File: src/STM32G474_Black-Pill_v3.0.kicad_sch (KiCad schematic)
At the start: 47 parts, among them J101 USB_C_Receptacle_USB2.0, J102 Conn_01x20, J103 Conn_01x20, J104 Conn_01x04, SW101 SW_Push, SW102 SW_Push, SW103 SW_Push, U101 W25Q32JVSS, U102 STM32G474CEUx, U103 AP7343xx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

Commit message: Add: Production data
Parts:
- C101, C104, C112, C114, C115, C119, C120: Manufacturer Part no. (none) -> -; Vendor (none) -> From stock; Vendor Part No. (none) -> -
- JP101, JP102, JP103: Manufacturer Part no. (none) -> -; Vendor (none) -> -; Vendor Part No. (none) -> -
- U102: Manufacturer Part no. (none) -> STM32G474CEU6; Vendor (none) -> Digikey; Vendor Part No. (none) -> 497-STM32G474CEU6-ND
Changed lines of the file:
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@@
+      (effects (font (size 1.27 1.27)) hide)
+    )
+    (property "Manufacturer Part no." "-" (at 133.35 184.15 0)
+      (effects (font (size 1.27 1.27)) hide)
+    )
+    (property "Vendor" "From stock" (at 133.35 184.15 0)
+      (effects (font (size 1.27 1.27)) hide)
+    )
+    (property "Vendor Part No." "-" (at 133.35 184.15 0)
       (effects (font (size 1.27 1.27)) hide)
     )
@@
     )
     (property "Datasheet" "~" (at 31.75 184.15 0)
+      (effects (font (size 1.27 1.27)) hide)
+    )
+    (property "Manufacturer Part no." "-" (at 31.75 184.15 0)
+      (effects (font (size 1.27 1.27)) hide)
+    )
+    (property "Vendor" "From stock" (at 31.75 184.15 0)
+      (effects (font (size 1.27 1.27)) hide)
+    )
+    (property "Vendor Part No." "-" (at 31.75 184.15 0)
       (effects (font (size 1.27 1.27)) hide)
     )
@@
       (effects (font (size 1.27 1.27)) hide)
     )
+    (property "Manufacturer Part no." "-" (at 63.5 184.15 0)
+      (effects (font (size 1.27 1.27)) hide)
+    )
+    (property "Vendor" "From stock" (at 63.5 184.15 0)
+      (effects (font (size 1.27 1.27)) hide)
+    )
+    (property "Vendor Part No." "-" (at 63.5 184.15 0)
+      (effects (font (size 1.27 1.27)) hide)
+    )
     (pin "1")
     (pin "2")
@@
       (effects (font (size 1.27 1.27)) hide)
     )
+    (property "Manufacturer Part no." "-" (at 102.87 90.17 0)
+      (effects (font (size 1.27 1.27)) hide)
+    )
+    (property "Vendor" "-" (at 102.87 90.17 0)
+      (effects (font (size 1.27 1.27)) hide)
+    )
+    (property "Vendor Part No." "-" (at 102.87 90.17 0)
+      (effects (font (size 1.27 1.27)) hide)
+    )
     (pin "1")
     (pin "2")
@@
     )
     (property "Datasheet" "https://www.st.com/resource/en/datasheet/stm32g474ce.pdf" (at 165.1 86.36 0)
+      (effects (font (size 1.27 1.27)) hide)
+    )
+    (property "Manufacturer Part no." "STM32G474CEU6" (at 165.1 86.36 0)
+      (effects (font (size 1.27 1.27)) hide)
+    )
+    (property "Vendor" "Digikey" (at 165.1 86.36 0)
+      (effects (font (size 1.27 1.27)) hide)
+    )
+    (property "Vendor Part No." "497-STM32G474CEU6-ND" (at 165.1 86.36 0)
       (effects (font (size 1.27 1.27)) hide)
     )
@@
       (effects (font (size 1.27 1.27)) hide)
     )
+    (property "Manufacturer Part no." "-" (at 110.49 24.13 0)
+      (effects (font (size 1.27 1.27)) hide)
+    )
+    (property "Vendor" "From stock" (at 110.49 24.13 0)
+      (effects (font (size 1.27 1.27)) hide)
+    )
+    (property "Vendor Part No." "-" (at 110.49 24.13 0)
+      (effects (font (size 1.27 1.27)) hide)
+    )
     (pin "1")
     (pin "2")
@@
       (effects (font (size 1.27 1.27)) hide)
     )
+    (property "Manufacturer Part no." "-" (at 146.05 184.15 0)
+      (effects (font (size 1.27 1.27)) hide)
+    )
+    (property "Vendor" "From stock" (at 146.05 184.15 0)
+      (effects (font (size 1.27 1.27)) hide)
+    )
+    (property "Vendor Part No." "-" (at 146.05 184.15 0)
+      (effects (font (size 1.27 1.27)) hide)
+    )
     (pin "1")
     (pin "2")
@@
     )
     (property "Datasheet" "~" (at 102.87 109.22 0)
+      (effects (font (size 1.27 1.27)) hide)
+    )
+    (property "Manufacturer Part no." "-" (at 102.87 109.22 0)
+      (effects (font (size 1.27 1.27)) hide)
+    )
+    (property "Vendor" "-" (at 102.87 109.22 0)
+      (effects (font (size 1.27 1.27)) hide)
+    )
+    (property "Vendor Part No." "-" (at 102.87 109.22 0)
       (effects (font (size 1.27 1.27)) hide)
     )
@@
       (effects (font (size 1.27 1.27)) hide)
     )
+    (property "Manufacturer Part no." "-" (at 264.16 45.72 0)
+      (effects (font (size 1.27 1.27)) hide)
+    )
+    (property "Vendor" "From stock" (at 264.16 45.72 0)
+      (effects (font (size 1.27 1.27)) hide)
+    )
+    (property "Vendor Part No." "-" (at 264.16 45.72 0)
+      (effects (font (size 1.27 1.27)) hide)
+    )
     (pin "1")
     (pin "2")
@@
       (effects (font (size 1.27 1.27)) hide)
     )
+    (property "Manufacturer Part no." "-" (at 107.95 152.4 0)
+      (effects (font (size 1.27 1.27)) hide)
+    )
+    (property "Vendor" "From stock" (at 107.95 152.4 0)
+      (effects (font (size 1.27 1.27)) hide)
+    )
+    (property "Vendor Part No." "-" (at 107.95 152.4 0)
+      (effects (font (size 1.27 1.27)) hide)
+    )
     (pin "1")
     (pin "2")
@@
       (effects (font (size 1.27 1.27)) hide)
     )
+    (property "Manufacturer Part no." "-" (at 67.31 146.05 0)
+      (effects (font (size 1.27 1.27)) hide)
+    )
+    (property "Vendor" "-" (at 67.31 146.05 0)
+      (effects (font (size 1.27 1.27)) hide)
+    )
+    (property "Vendor Part No." "-" (at 67.31 146.05 0)
+      (effects (font (size 1.27 1.27)) hide)
+    )

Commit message: Mod: STM32G474_Black-Pill_v3.0.kicad_sch, updated BOM and re-exported BOM_A.xlsx.
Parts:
- C101, C104, C108, C109, C110, C112, C114, C115, C119, C120: Manufacturer Part no. - -> GRM155R71C104KA88D; Vendor From stock -> Digikey; Vendor Part No. - -> 490-3261-1-ND
- C107: Manufacturer Part no. - -> GRM155R60J106ME15D; Vendor From stock -> Digikey; Vendor Part No. - -> 490-13238-1-ND
- C113, C116, C117, C118: Manufacturer Part no. - -> GRM155C81C105KE11D; Vendor From stock -> Digikey; Vendor Part No. - -> 490-12700-1-ND
- R101, R102: Manufacturer Part no. - -> RC0402FR-075K1L; Vendor From stock -> Digikey; Vendor Part No. - -> 311-5.10KLRCT-ND
- R103, R108: Manufacturer Part no. - -> RC0402FR-0710KL; Vendor From stock -> Digikey; Vendor Part No. - -> 311-10.0KLRCT-ND
- R104, R105: Manufacturer Part no. - -> RC0402FR-0710RL; Vendor From stock -> Digikey; Vendor Part No. - -> 311-10.0LRCT-ND
- R107, R109: Manufacturer Part no. - -> RC0402FR-07100RL; Vendor From stock -> Digikey; Vendor Part No. - -> 311-100LRCT-ND
- R218: Manufacturer Part no. - -> RC0402FR-070RL; Vendor From stock -> Digikey; Vendor Part No. - -> 311-0.0LRCT-ND

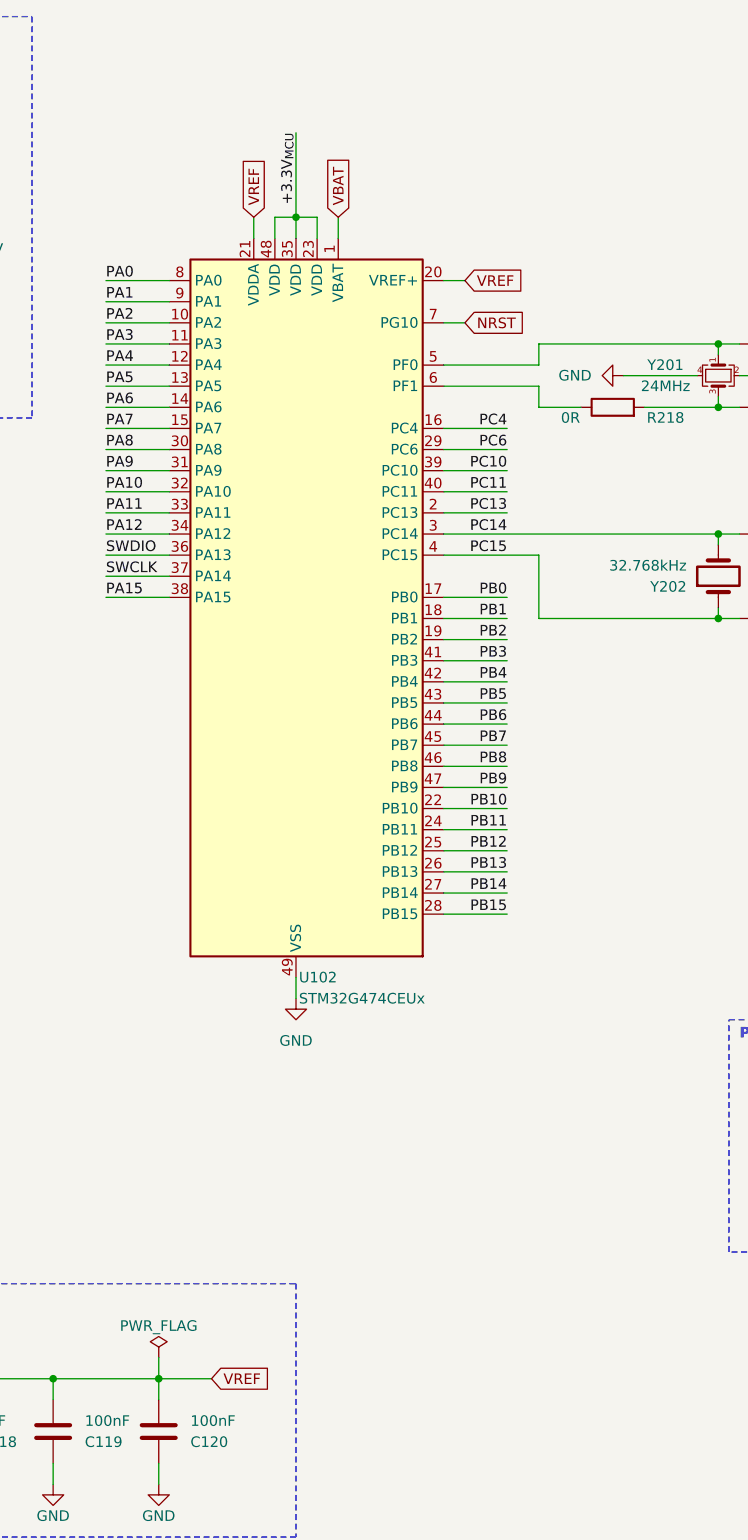
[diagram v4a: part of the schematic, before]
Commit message: Mod: Schematic_A.pdf, renamed VREF to VDDA
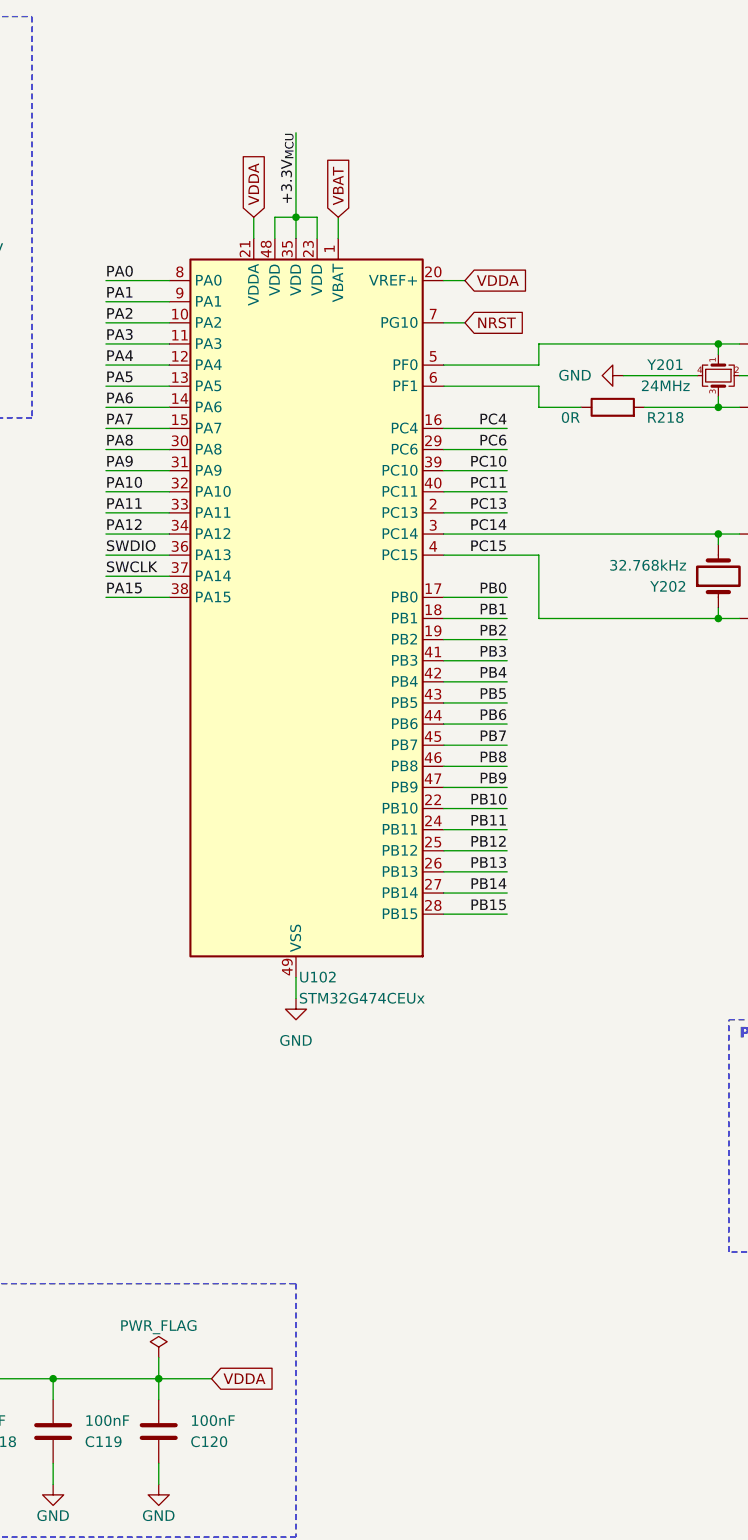
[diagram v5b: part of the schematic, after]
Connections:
- net VREF renamed VDDA
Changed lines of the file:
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@@
     (effects (font (size 1.27 1.27)) (justify left bottom))
   )
-  (global_label "VREF" (shape input) (at 182.88 45.72 0) (fields_autoplaced)
+  (global_label "VDDA" (shape input) (at 182.88 45.72 0) (fields_autoplaced)
     (effects (font (size 1.27 1.27)) (justify left))
-    (property "Intersheetrefs" "${INTERSHEET_REFS}" (at 190.4614 45.72 0)
+    (property "Intersheetrefs" "${INTERSHEET_REFS}" (at 190.5824 45.72 0)
       (effects (font (size 1.27 1.27)) (justify left) hide)
     )
@@
     )
   )
-  (global_label "VREF" (shape input) (at 152.4 177.8 0) (fields_autoplaced)
+  (global_label "VDDA" (shape input) (at 152.4 177.8 0) (fields_autoplaced)
     (effects (font (size 1.27 1.27)) (justify left))
-    (property "Intersheetrefs" "${INTERSHEET_REFS}" (at 159.9814 177.8 0)
+    (property "Intersheetrefs" "${INTERSHEET_REFS}" (at 160.1024 177.8 0)
       (effects (font (size 1.27 1.27)) (justify left) hide)
     )
@@
     )
   )
-  (global_label "VREF" (shape input) (at 157.48 38.1 90) (fields_autoplaced)
+  (global_label "VDDA" (shape input) (at 157.48 38.1 90) (fields_autoplaced)
     (effects (font (size 1.27 1.27)) (justify left))
-    (property "Intersheetrefs" "${INTERSHEET_REFS}" (at 157.48 30.5186 90)
-      (effects (font (size 1.27 1.27)) (justify right) hide)
+    (property "Intersheetrefs" "${INTERSHEET_REFS}" (at 157.48 30.3976 90)
+      (effects (font (size 1.27 1.27)) (justify left) hide)
     )
   )
